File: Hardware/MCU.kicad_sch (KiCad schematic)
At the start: 30 parts, among them IC1 SN74AHC1G32DBVR, J3 SWD, SW1 RST, SW2 BOOT, U5 STM32L431CBTx, Y1 8M

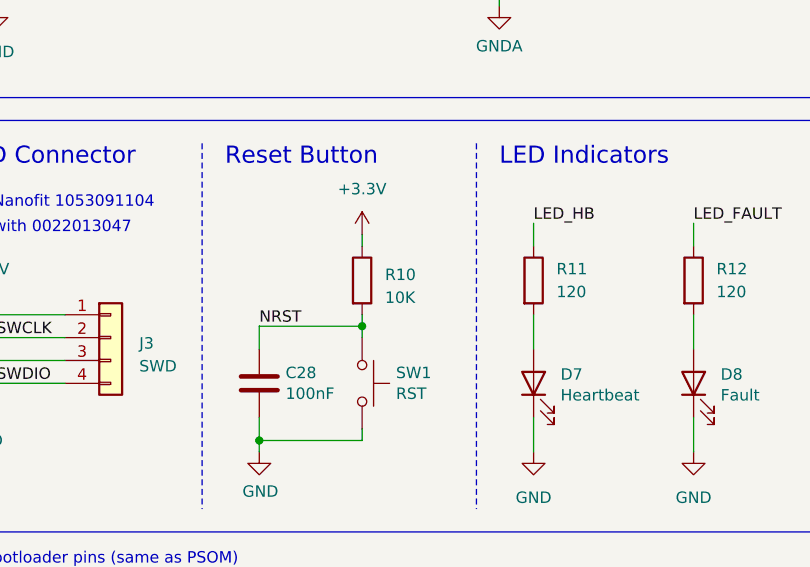
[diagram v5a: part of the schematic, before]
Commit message: updated some component part nums
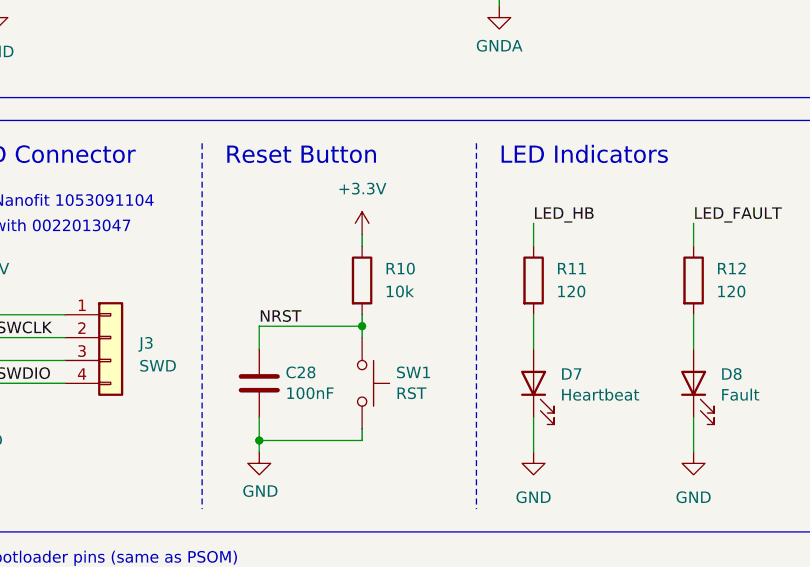
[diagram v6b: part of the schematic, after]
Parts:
- C19: Mfg (none) -> 08055D475KAT4A
- C20, C21, C22, C23, C24, C26, C28, C29: Mfg (none) -> MLASH168SB7104KTNA01; P/N C0805C104M5RACTU -> MLASH168SB7104KTNA01
- C25, C27: Mfg (none) -> 06035U120FAT2A; P/N C0805C120K5HACTU -> 06035U120FAT2A
- R10: value 10K -> 10k; Mfg (none) -> CRCW060310K0FKEI; P/N CRCW080510K0FKEAC -> CRCW060310K0FKEI
- R11, R12, R13, R14: Mfg (none) -> CRCW0603120RFKEC; P/N (none) -> CRCW0603120RFKEC
- R15: Mfg (none) -> CRCW060310K0FKEI
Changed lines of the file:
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@@
 			)
 		)
-		(property "P/N" "C0805C104M5RACTU"
+		(property "P/N" "MLASH168SB7104KTNA01"
 			(at 184.15 82.55 0)
 			(effects
@@
 			)
 		)
+		(property "Mfg" "MLASH168SB7104KTNA01"
+			(at 184.15 82.55 0)
+			(effects
+				(font
+					(size 1.27 1.27)
+				)
+				(hide yes)
+			)
+		)
 		(pin "1"
 		)
@@
 			)
 		)
-		(property "P/N" "C0805C104M5RACTU"
+		(property "P/N" "MLASH168SB7104KTNA01"
 			(at 259.08 38.1 0)
 			(effects
@@
 			)
 		)
+		(property "Mfg" "MLASH168SB7104KTNA01"
+			(at 259.08 38.1 0)
+			(effects
+				(font
+					(size 1.27 1.27)
+				)
+				(hide yes)
+			)
+		)
 		(pin "1"
 		)
@@
 			)
 		)
-		(property "P/N" "C0805C104M5RACTU"
+		(property "P/N" "MLASH168SB7104KTNA01"
 			(at 190.5 35.56 0)
 			(effects
@@
 			)
 		)
+		(property "Mfg" "MLASH168SB7104KTNA01"
+			(at 190.5 35.56 0)
+			(effects
+				(font
+					(size 1.27 1.27)
+				)
+				(hide yes)
+			)
+		)
 		(pin "1"
 		)
@@
 			)
 		)
+		(property "Mfg" "CRCW0603120RFKEC "
+			(at 232.41 71.12 0)
+			(effects
+				(font
+					(size 1.27 1.27)
+				)
+				(hide yes)
+			)
+		)
+		(property "P/N" "CRCW0603120RFKEC "
+			(at 232.41 71.12 0)
+			(effects
+				(font
+					(size 1.27 1.27)
+				)
+				(hide yes)
+			)
+		)
 		(pin "1"
 		)
@@
 			)
 		)
-		(property "P/N" "C0805C120K5HACTU"
+		(property "P/N" "06035U120FAT2A"
 			(at 29.21 46.99 0)
 			(effects
@@
 			)
 		)
+		(property "Mfg" "06035U120FAT2A"
+			(at 29.21 46.99 90)
+			(effects
+				(font
+					(size 1.27 1.27)
+				)
+				(hide yes)
+			)
+		)
 		(pin "1"
 		)
@@
 			)
 		)
-		(property "P/N" "C0805C104M5RACTU"
+		(property "P/N" "MLASH168SB7104KTNA01"
 			(at 210.82 35.56 0)
 			(effects
@@
 			)
 		)
+		(property "Mfg" "MLASH168SB7104KTNA01"
+			(at 210.82 35.56 0)
+			(effects
+				(font
+					(size 1.27 1.27)
+				)
+				(hide yes)
+			)
+		)
 		(pin "1"
 		)
@@
 			)
 		)
+		(property "Mfg" "CRCW0603120RFKEC "
+			(at 247.65 71.12 0)
+			(effects
+				(font
+					(size 1.27 1.27)
+				)
+				(hide yes)
+			)
+		)
+		(property "P/N" "CRCW0603120RFKEC "
+			(at 247.65 71.12 0)
+			(effects
+				(font
+					(size 1.27 1.27)
+				)
+				(hide yes)
+			)
+		)
 		(pin "1"
 		)
@@
 			)
 		)
-		(property "P/N" "C0805C104M5RACTU"
+		(property "P/N" "MLASH168SB7104KTNA01"
 			(at 166.37 35.56 0)
 			(effects
@@
 			)
 		)
+		(property "Mfg" "MLASH168SB7104KTNA01"
+			(at 166.37 35.56 0)
+			(effects
+				(font
+					(size 1.27 1.27)
+				)
+				(hide yes)
+			)
+		)
 		(pin "1"
 		)
@@
 			)
 		)
+		(property "Mfg" "CRCW0603120RFKEC "
+			(at 262.89 71.12 0)
+			(effects
+				(font
+					(size 1.27 1.27)
+				)
+				(hide yes)
+			)
+		)
+		(property "P/N" "CRCW0603120RFKEC "
+			(at 262.89 71.12 0)
+			(effects
+				(font
+					(size 1.27 1.27)
+				)
+				(hide yes)
+			)
+		)
 		(pin "1"
 		)
@@
 			)
 		)
-		(property "P/N" "C0805C104M5RACTU"
+		(property "P/N" "MLASH168SB7104KTNA01"
 			(at 226.06 35.56 0)
 			(effects
@@
 			)
 		)
+		(property "Mfg" "MLASH168SB7104KTNA01"
+			(at 226.06 35.56 0)
+			(effects
+				(font
+					(size 1.27 1.27)
+				)
+				(hide yes)
+			)
+		)
 		(pin "1"
 		)
@@
 			)
 		)
+		(property "Mfg" "CRCW0603120RFKEC "
+			(at 214.63 71.12 0)
+			(effects
+				(font
+					(size 1.27 1.27)
+				)
+				(hide yes)
+			)
+		)
+		(property "P/N" "CRCW0603120RFKEC "
+			(at 214.63 71.12 0)
+			(effects
+				(font
+					(size 1.27 1.27)
+				)
+				(hide yes)
+			)
+		)
 		(pin "1"
 		)
@@
 		(fields_autoplaced yes)
 		(property "Reference" "R10"
-			(at 198.12 70.485 0)
+			(at 198.12 69.8499 0)
 			(effects
 				(font
@@
 			)
 		)
-		(property "Value" "10K"
-			(at 198.12 73.025 0)
+		(property "Value" "10k"
+			(at 198.12 72.3899 0)
 			(effects
 				(font
@@
 			)
 		)
-		(property "P/N" "CRCW080510K0FKEAC"
+		(property "P/N" "CRCW060310K0FKEI "
 			(at 195.58 71.12 0)
 			(effects
@@
 			)
 		)
+		(property "Mfg" "CRCW060310K0FKEI "
+			(at 195.58 71.12 0)
+			(effects
+				(font
+					(size 1.27 1.27)
+				)
+				(hide yes)
+			)
+		)
 		(pin "1"
 		)
@@
 			)
 		)
-		(property "P/N" "C0805C104M5RACTU"
+		(property "P/N" "MLASH168SB7104KTNA01"
 			(at 177.8 35.56 0)
 			(effects
@@
 			)
 		)
+		(property "Mfg" "MLASH168SB7104KTNA01"
+			(at 177.8 35.56 0)
+			(effects
+				(font
+					(size 1.27 1.27)
+				)
+				(hide yes)
+			)
+		)
 		(pin "1"
 		)
@@
 			)
 		)
-		(property "P/N" "C0805C120K5HACTU"
+		(property "P/N" "06035U120FAT2A"
 			(at 29.21 36.83 0)
 			(effects
@@
 			)
 		)
+		(property "Mfg" "06035U120FAT2A"
+			(at 29.21 36.83 90)
+			(effects
+				(font
+					(size 1.27 1.27)
+				)
+				(hide yes)
+			)
+		)
 		(pin "1"
 		)
@@
 			)
 		)
+		(property "Mfg" "08055D475KAT4A"
+			(at 154.94 35.56 0)
+			(effects
+				(font
+					(size 1.27 1.27)
+				)
+				(hide yes)
+			)
+		)
 		(pin "1"
 		)
@@
 			)
 		)
+		(property "Mfg" "CRCW060310K0FKEI "
+			(at 220.98 132.08 90)
+			(effects
+				(font
+					(size 1.27 1.27)
+				)
+				(hide yes)
+			)
+		)
 		(pin "1"
 		)
@@
 			)
 		)
-		(property "P/N" "C0805C104M5RACTU"
+		(property "P/N" "MLASH168SB7104KTNA01"
 			(at 213.36 137.16 0)
 			(effects
@@
 			(at 213.36 137.16 0)
 			(effects
+				(font
+					(size 1.27 1.27)
+				)
+				(hide yes)
+			)
+		)
+		(property "Mfg" "MLASH168SB7104KTNA01"
+			(at 213.36 137.16 0)
+			(effects

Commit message: generated production stuff
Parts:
- D10, D7, D9: P/N (none) -> XL-1608UBC-06A
- D8: P/N (none) -> NCD0603R1
- IC1: P/N (none) -> SN74AHC1G32DBVR
- SW1: Mfg (none) -> TL3365AF180QG
- SW2: Mfg (none) -> CJS-1200TA
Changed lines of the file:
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@@
+			)
+		)
+		(property "P/N" "NCD0603R1"
+			(at 232.41 82.55 90)
+			(effects
+				(font
+					(size 1.27 1.27)
+				)
+				(hide yes)
 			)
 		)
@@
 		(property "Sim.Pins" "1=K 2=A"
 			(at 214.63 82.55 0)
+			(effects
+				(font
+					(size 1.27 1.27)
+				)
+				(hide yes)
+			)
+		)
+		(property "P/N" "XL-1608UBC-06A"
+			(at 214.63 82.55 90)
 			(effects
 				(font
@@
 			)
 		)
+		(property "Mfg" "CJS-1200TA "
+			(at 171.45 129.54 0)
+			(effects
+				(font
+					(size 1.27 1.27)
+				)
+				(hide yes)
+			)
+		)
 		(pin "2"
 		)
@@
 			)
 		)
+		(property "P/N" "XL-1608UBC-06A"
+			(at 247.65 82.55 90)
+			(effects
+				(font
+					(size 1.27 1.27)
+				)
+				(hide yes)
+			)
+		)
 		(pin "1"
 		)
@@
 		)
 		(property "P/N" "TL3365AF180QG"
+			(at 195.58 82.55 90)
+			(effects
+				(font
+					(size 1.27 1.27)
+				)
+				(hide yes)
+			)
+		)
+		(property "Mfg" "TL3365AF180QG"
 			(at 195.58 82.55 90)
 			(effects
@@
 			)
 		)
+		(property "P/N" "XL-1608UBC-06A"
+			(at 262.89 82.55 90)
+			(effects
+				(font
+					(size 1.27 1.27)
+				)
+				(hide yes)
+			)
+		)
 		(pin "1"
 		)
@@
 				(hide yes)
 			)
+		)
+		(property "P/N" "SN74AHC1G32DBVR"
+			(at 186.69 129.54 0)
+			(effects
+				(font
+					(size 1.27 1.27)
+				)
+				(hide yes)
+			)
